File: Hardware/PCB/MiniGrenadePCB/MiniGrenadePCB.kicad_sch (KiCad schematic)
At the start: 3 parts, among them U1 DF-Player_mini, U2 WeMos_D1_mini

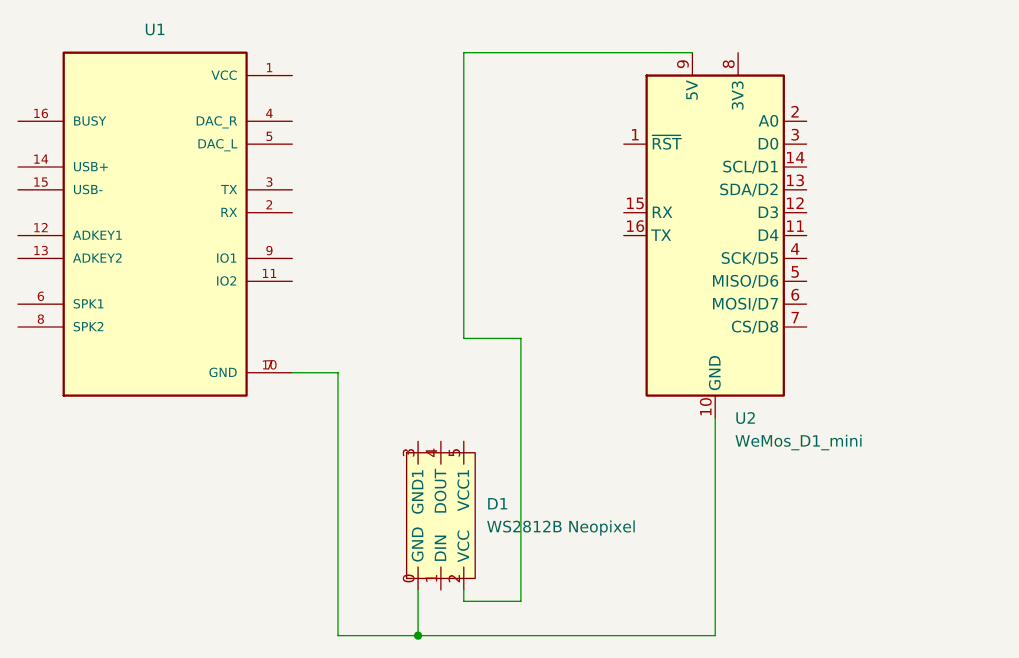
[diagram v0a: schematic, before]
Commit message: Started working on the bayonet for the mini grenade
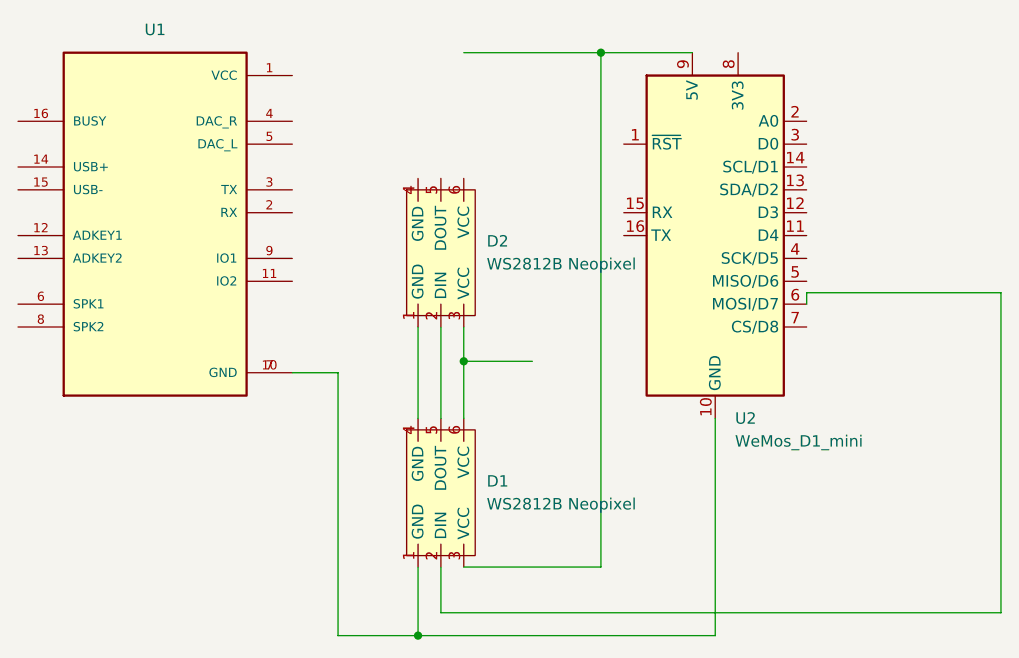
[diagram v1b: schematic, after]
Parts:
- added D2: WS2812B Neopixel, Grenade_Stuff:NeoPixel_strip, symbol GrenadeStuff:NeoPixelStrip
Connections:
- net at U1.10 (GND), U1.7 (GND), U2.10 (GND): now also D1.1 (GND); no longer D1.0 (GND)
- net at D1.2 (DIN): now also U2.6 (MOSI/D7); no longer U2.9 (5V)
- net at D1.3 (VCC): now also U2.9 (5V)
- net at D1.4 (GND): now also D2.1 (GND)
- net at D1.5 (DOUT): now also D2.2 (DIN)
- new net: D1.6 (VCC), D2.3 (VCC)
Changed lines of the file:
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@@
 (kicad_sch (version 20230121) (generator eeschema)
   (paper "A4")
+  (junction (at 170.18 107.95) (diameter 0) (color 0 0 0 0)
+  )
+  (junction (at 185.42 73.66) (diameter 0) (color 0 0 0 0)
+  )
   (junction (at 165.1 138.43) (diameter 0) (color 0 0 0 0)
+  )
+  (wire (pts (xy 185.42 130.81) (xy 185.42 73.66))
+    (stroke (width 0) (type default))
+  )
+  (wire (pts (xy 165.1 130.81) (xy 165.1 138.43))
+    (stroke (width 0) (type default))
+  )
+  (wire (pts (xy 165.1 138.43) (xy 198.12 138.43))
+    (stroke (width 0) (type default))
   )
   (wire (pts (xy 198.12 138.43) (xy 198.12 114.3))
     (stroke (width 0) (type default))
   )
-  (wire (pts (xy 170.18 73.66) (xy 170.18 105.41))
+  (wire (pts (xy 170.18 73.66) (xy 185.42 73.66))
     (stroke (width 0) (type default))
   )
-  (wire (pts (xy 176.53 105.41) (xy 176.53 134.62))
+  (wire (pts (xy 229.87 100.33) (xy 208.28 100.33))
     (stroke (width 0) (type default))
   )
-  (wire (pts (xy 170.18 105.41) (xy 176.53 105.41))
+  (wire (pts (xy 167.64 104.14) (xy 167.64 114.3))
     (stroke (width 0) (type default))
   )
-  (wire (pts (xy 170.18 73.66) (xy 195.58 73.66))
-    (stroke (width 0) (type default))
-  )
-  (wire (pts (xy 165.1 138.43) (xy 165.1 133.35))
+  (wire (pts (xy 170.18 104.14) (xy 170.18 107.95))
     (stroke (width 0) (type default))
   )
@@
     (stroke (width 0) (type default))
   )
-  (wire (pts (xy 170.18 134.62) (xy 170.18 133.35))
+  (wire (pts (xy 167.64 135.89) (xy 229.87 135.89))
+    (stroke (width 0) (type default))
+  )
+  (wire (pts (xy 229.87 135.89) (xy 229.87 100.33))
+    (stroke (width 0) (type default))
+  )
+  (wire (pts (xy 156.21 138.43) (xy 165.1 138.43))
+    (stroke (width 0) (type default))
+  )
+  (wire (pts (xy 165.1 104.14) (xy 165.1 114.3))
+    (stroke (width 0) (type default))
+  )
+  (wire (pts (xy 208.28 100.33) (xy 208.28 101.6))
     (stroke (width 0) (type default))
   )
@@
     (stroke (width 0) (type default))
   )
-  (wire (pts (xy 165.1 138.43) (xy 198.12 138.43))
+  (wire (pts (xy 185.42 73.66) (xy 195.58 73.66))
     (stroke (width 0) (type default))
   )
-  (wire (pts (xy 156.21 138.43) (xy 165.1 138.43))
+  (wire (pts (xy 170.18 107.95) (xy 170.18 114.3))
     (stroke (width 0) (type default))
   )
-  (wire (pts (xy 176.53 134.62) (xy 170.18 134.62))
+  (wire (pts (xy 167.64 130.81) (xy 167.64 135.89))
     (stroke (width 0) (type default))
   )
-  (symbol (lib_id "GrenadeStuff:NeoPixelStrip") (at 167.64 129.54 0) (unit 1)
+  (wire (pts (xy 170.18 130.81) (xy 185.42 130.81))
+    (stroke (width 0) (type default))
+  )
+  (wire (pts (xy 170.18 107.95) (xy 177.8 107.95))
+    (stroke (width 0) (type default))
+  )
+  (symbol (lib_id "GrenadeStuff:NeoPixelStrip") (at 167.64 100.33 0) (unit 1)
     (in_bom yes) (on_board yes) (dnp no) (fields_autoplaced)
-    (property "Reference" "D1" (at 172.72 123.825 0)
+    (property "Reference" "D2" (at 172.72 94.615 0)
       (effects (font (size 1.27 1.27)) (justify left))
     )
-    (property "Value" "WS2812B Neopixel" (at 172.72 126.365 0)
+    (property "Value" "WS2812B Neopixel" (at 172.72 97.155 0)
       (effects (font (size 1.27 1.27)) (justify left))
     )
-    (property "Footprint" "Grenade_Stuff:NeoPixel_strip" (at 167.64 129.54 0)
+    (property "Footprint" "Grenade_Stuff:NeoPixel_strip" (at 167.64 100.33 0)
       (effects (font (size 1.27 1.27)) hide)
     )
-    (property "Datasheet" "" (at 167.64 129.54 0)
+    (property "Datasheet" "" (at 167.64 100.33 0)
       (effects (font (size 1.27 1.27)) hide)
     )
+    (pin "4")
+    (pin "6")
     (pin "5")
     (pin "2")
-    (pin "4")
     (pin "3")
-    (pin "0")
     (pin "1")
     (instances
       (project "MiniGrenadePCB"
         (path "/903d1f49-37b0-45d7-9079-bf49af1c090a"
-          (reference "D1") (unit 1)
+          (reference "D2") (unit 1)
         )
       )
@@
         )
       )
+    )
+  )
+  (symbol (lib_id "GrenadeStuff:NeoPixelStrip") (at 167.64 127 0) (unit 1)
+    (in_bom yes) (on_board yes) (dnp no) (fields_autoplaced)
+    (property "Reference" "D1" (at 172.72 121.285 0)
+      (effects (font (size 1.27 1.27)) (justify left))
+    )
+    (property "Value" "WS2812B Neopixel" (at 172.72 123.825 0)
+      (effects (font (size 1.27 1.27)) (justify left))
+    )
+    (property "Footprint" "Grenade_Stuff:NeoPixel_strip" (at 167.64 127 0)
+      (effects (font (size 1.27 1.27)) hide)
+    )
+    (property "Datasheet" "" (at 167.64 127 0)
+      (effects (font (size 1.27 1.27)) hide)
+    )
+    (pin "4")
+    (pin "6")
+    (pin "5")
+    (pin "2")
+    (pin "3")
+    (pin "1")
+    (instances
+      (project "MiniGrenadePCB"
+        (path "/903d1f49-37b0-45d7-9079-bf49af1c090a"
+          (reference "D1") (unit 1)
+        )
+      )
